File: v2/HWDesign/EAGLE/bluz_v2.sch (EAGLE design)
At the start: 24 parts, among them Q1 FC-12M, U1 MDBT40SMD, U2 SST25VF016B-50-4I-S2AF, U3 MCP1700T-3302E/TT

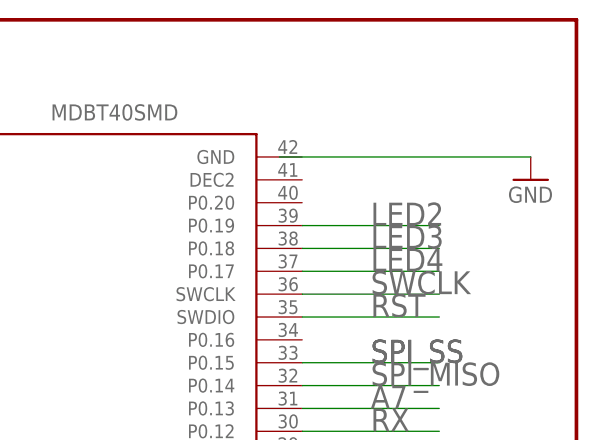
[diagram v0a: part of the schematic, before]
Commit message: fix an issue on the PCB
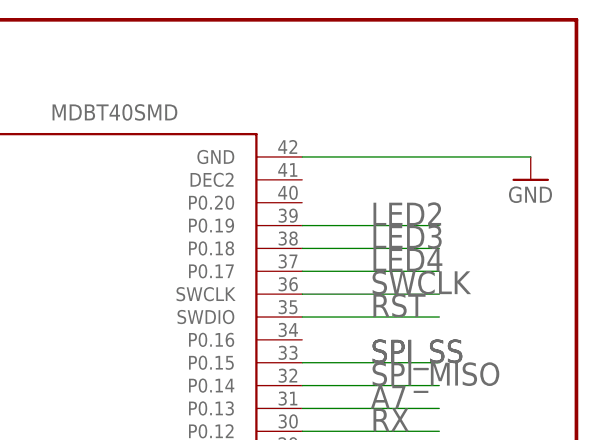
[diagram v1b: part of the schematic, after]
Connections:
- net GND: now also U1.GND@5
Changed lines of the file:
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@@
-</segment>
-<segment>
-<pinref part="GND7" gate="1" pin="GND"/>
-<wire x1="246.38" y1="200.66" x2="274.32" y2="200.66" width="0.1524" layer="91"/>
 </segment>
 <segment>
@@
 <wire x1="193.04" y1="119.38" x2="193.04" y2="124.46" width="0.1524" layer="91"/>
 </segment>
+<segment>
+<pinref part="U1" gate="G$1" pin="GND@5"/>
+<pinref part="GND7" gate="1" pin="GND"/>
+<wire x1="248.92" y1="200.66" x2="274.32" y2="200.66" width="0.1524" layer="91"/>
+</segment>
 </net>

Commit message: larger silkscreen. remove labels. copper on bottom of castellated edges. move buttons further in
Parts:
- removed U2: SST25VF016B-50-4I-S2AF, Silicon_Storage_Tech_By_element14_Batch_1:SST25VF016B-50-4I-S2AF
- added U4: SST25VF010A-33-4I-SAE, Silicon_Storage_Tech_By_element14_Batch_1:SST25VF010A-33-4I-SAE
- R1: value (none) -> 1k
- R6: value (none) -> 10k
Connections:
- net GND: now also U4.VSS; no longer U2.VSS
- net SPI_MISO: now also U4.SO; no longer U2.SO
- net SPI_MOSI: now also U4.SI; no longer U2.SI
- net SPI_SCK: now also U4.SCK; no longer U2.SCK
- net SPI_SS: now also U4.CE; no longer U2.CE
- net VCC: now also U4.HOLD, U4.VDD, U4.WP; no longer U2.HOLD, U2.VDD, U2.WP
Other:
- note added: "C"
- note removed: "A"
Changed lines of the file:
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@@
 <?xml version="1.0" encoding="utf-8"?>
 <!DOCTYPE eagle SYSTEM "eagle.dtd">
-<eagle version="6.5.0">
+<eagle version="7.3.0">
 <drawing>
 <settings>
@@
 <parts>
 <part name="U1" library="MDBT40" deviceset="MDBT40" device="SMD"/>
-<part name="U2" library="Silicon_Storage_Tech_By_element14_Batch_1" deviceset="SST25VF016B-50-4I-S2AF" device="" value=""/>
 <part name="GND1" library="SparkFun-Aesthetics" deviceset="GND" device=""/>
 <part name="C1" library="SparkFun-Capacitors" deviceset="CAP" device="0603-CAP" value="1uF"/>
@@
 <part name="GND3" library="SparkFun-Aesthetics" deviceset="GND" device=""/>
 <part name="C3" library="SparkFun-Capacitors" deviceset="CAP" device="0603-CAP" value=".1uF"/>
-<part name="R1" library="SparkFun-Resistors" deviceset="RESISTOR" device="0603"/>
+<part name="R1" library="SparkFun-Resistors" deviceset="RESISTOR" device="0603" value="1k"/>
 <part name="SUPPLY3" library="SparkFun-Aesthetics" deviceset="VCC" device=""/>
 <part name="GND4" library="SparkFun-Aesthetics" deviceset="GND" device=""/>
@@
 <part name="GND9" library="SparkFun-Aesthetics" deviceset="GND" device=""/>
 <part name="GND10" library="SparkFun-Aesthetics" deviceset="GND" device=""/>
-<part name="R6" library="SparkFun-Passives" deviceset="RESISTOR" device="0603-RES"/>
+<part name="R6" library="SparkFun-Passives" deviceset="RESISTOR" device="0603-RES" value="10k"/>
 <part name="SUPPLY5" library="SparkFun-Aesthetics" deviceset="VCC" device=""/>
 <part name="U3" library="Microchip_By_element14_Batch_1" deviceset="MCP1700T-3302E/TT" device=""/>
@@
 <part name="FRAME1" library="SparkFun-Aesthetics" deviceset="FRAME-LETTER" device=""/>
 <part name="SUPPLY6" library="SparkFun-Aesthetics" deviceset="VCC" device=""/>
+<part name="U4" library="Silicon_Storage_Tech_By_element14_Batch_1" deviceset="SST25VF010A-33-4I-SAE" device=""/>
 </parts>
 <sheets>
@@
 <text x="213.36" y="111.76" size="2.54" layer="95">MDBT40-256R</text>
 <text x="200.66" y="6.35" size="5.08" layer="94">Eric Ely</text>
-<text x="269.494" y="6.35" size="3.81" layer="94">A</text>
+<text x="269.494" y="6.35" size="3.81" layer="94">C</text>
 <text x="195.834" y="16.764" size="3.81" layer="94">Bluz DK v2</text>
 <text x="189.992" y="1.016" size="2.54" layer="94">July 1, 2015</text>
@@
 <instances>
 <instance part="U1" gate="G$1" x="220.98" y="177.8"/>
-<instance part="U2" gate="A" x="63.5" y="139.7"/>
 <instance part="GND1" gate="1" x="27.94" y="175.26"/>
 <instance part="C1" gate="G$1" x="17.78" y="187.96"/>
@@
 </instance>
 <instance part="SUPPLY6" gate="G$1" x="109.22" y="205.74"/>
+<instance part="U4" gate="A" x="63.5" y="139.7"/>
 </instances>
 <busses>
@@
 </segment>
 <segment>
-<pinref part="U2" gate="A" pin="VSS"/>
 <pinref part="GND3" gate="1" pin="GND"/>
 <wire x1="38.1" y1="127" x2="45.72" y2="127" width="0.1524" layer="91"/>
@@
 <junction x="38.1" y="127"/>
 <pinref part="C3" gate="G$1" pin="2"/>
+<pinref part="U4" gate="A" pin="VSS"/>
 </segment>
 <segment>
@@
 <segment>
 <pinref part="SUPPLY2" gate="G$1" pin="VCC"/>
-<pinref part="U2" gate="A" pin="VDD"/>
 <wire x1="7.62" y1="147.32" x2="25.4" y2="147.32" width="0.1524" layer="91"/>
 <wire x1="25.4" y1="147.32" x2="45.72" y2="147.32" width="0.1524" layer="91"/>
@@
 <wire x1="25.4" y1="134.62" x2="25.4" y2="132.08" width="0.1524" layer="91"/>
 <wire x1="25.4" y1="132.08" x2="45.72" y2="132.08" width="0.1524" layer="91"/>
+<junction x="25.4" y="134.62"/>
+<pinref part="C3" gate="G$1" pin="1"/>
 <wire x1="45.72" y1="132.08" x2="48.26" y2="132.08" width="0.1524" layer="91"/>
 <wire x1="48.26" y1="134.62" x2="45.72" y2="134.62" width="0.1524" layer="91"/>
-<junction x="25.4" y="134.62"/>
-<pinref part="C3" gate="G$1" pin="1"/>
 <wire x1="45.72" y1="134.62" x2="25.4" y2="134.62" width="0.1524" layer="91"/>
 <wire x1="7.62" y1="134.62" x2="7.62" y2="137.16" width="0.1524" layer="91"/>
@@
 <wire x1="12.7" y1="137.16" x2="7.62" y2="137.16" width="0.1524" layer="91"/>
 <junction x="7.62" y="137.16"/>
-<pinref part="U2" gate="A" pin="WP"/>
+<pinref part="U4" gate="A" pin="VDD"/>
+<pinref part="U4" gate="A" pin="WP"/>
 <junction x="45.72" y="134.62"/>
-<pinref part="U2" gate="A" pin="HOLD"/>
+<pinref part="U4" gate="A" pin="HOLD"/>
 <junction x="45.72" y="132.08"/>
 </segment>
@@
 <net name="SPI_SS" class="0">
 <segment>
-<pinref part="U2" gate="A" pin="CE"/>
 <pinref part="R1" gate="G$1" pin="2"/>
 <wire x1="45.72" y1="137.16" x2="22.86" y2="137.16" width="0.1524" layer="91"/>
 <label x="33.02" y="137.16" size="1.778" layer="95"/>
+<pinref part="U4" gate="A" pin="CE"/>
 </segment>
 <segment>
@@
 <net name="SPI_MOSI" class="0">
 <segment>
-<pinref part="U2" gate="A" pin="SI"/>
 <wire x1="45.72" y1="142.24" x2="35.56" y2="142.24" width="0.1524" layer="91"/>
 <label x="33.02" y="142.24" size="1.778" layer="95"/>
+<pinref part="U4" gate="A" pin="SI"/>
 </segment>
 <segment>
@@
 <net name="SPI_SCK" class="0">
 <segment>
-<pinref part="U2" gate="A" pin="SCK"/>
 <wire x1="45.72" y1="139.7" x2="35.56" y2="139.7" width="0.1524" layer="91"/>
 <label x="33.02" y="139.7" size="1.778" layer="95"/>
+<pinref part="U4" gate="A" pin="SCK"/>
 </segment>
 <segment>
@@
 <net name="SPI_MISO" class="0">
 <segment>
-<pinref part="U2" gate="A" pin="SO"/>
 <wire x1="81.28" y1="147.32" x2="93.98" y2="147.32" width="0.1524" layer="91"/>
 <label x="83.82" y="147.32" size="1.778" layer="95"/>
-</segment>
-<segment>
+<pinref part="U4" gate="A" pin="SO"/>
+</segment>
+<segment>

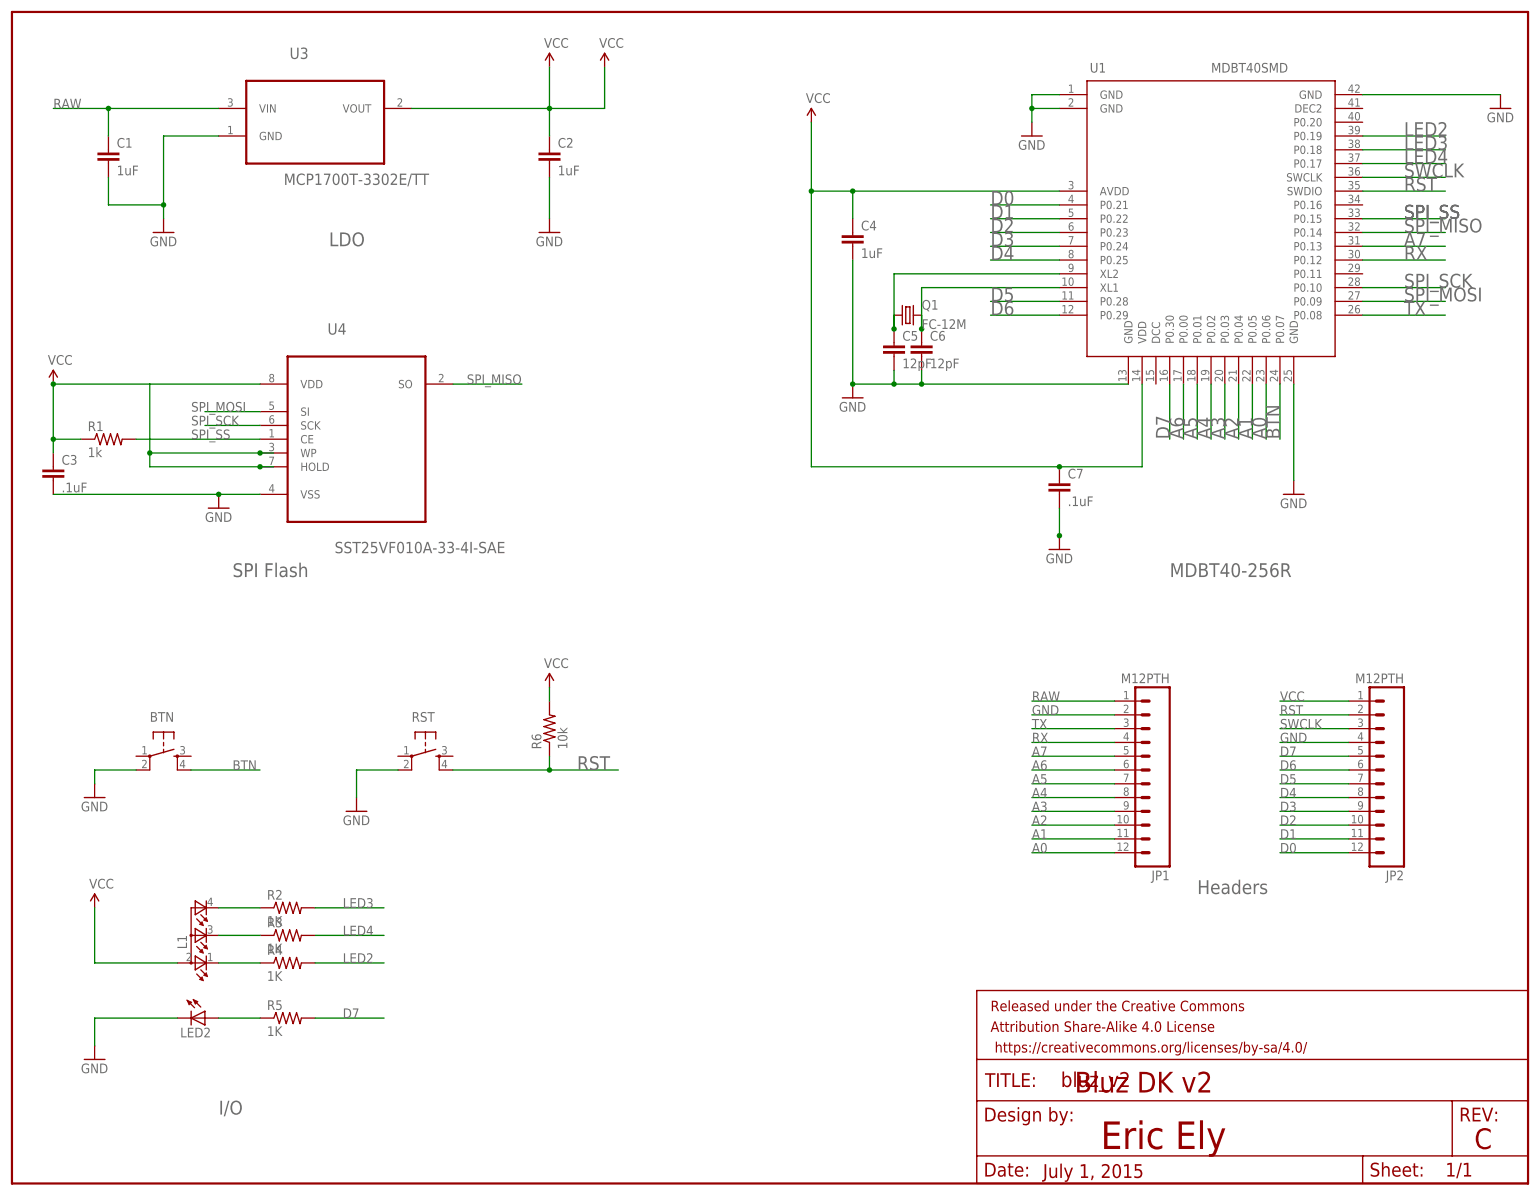
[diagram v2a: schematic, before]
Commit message: updated RGB LED to new part. changed resistors for new LED. updated labeling on bluz.
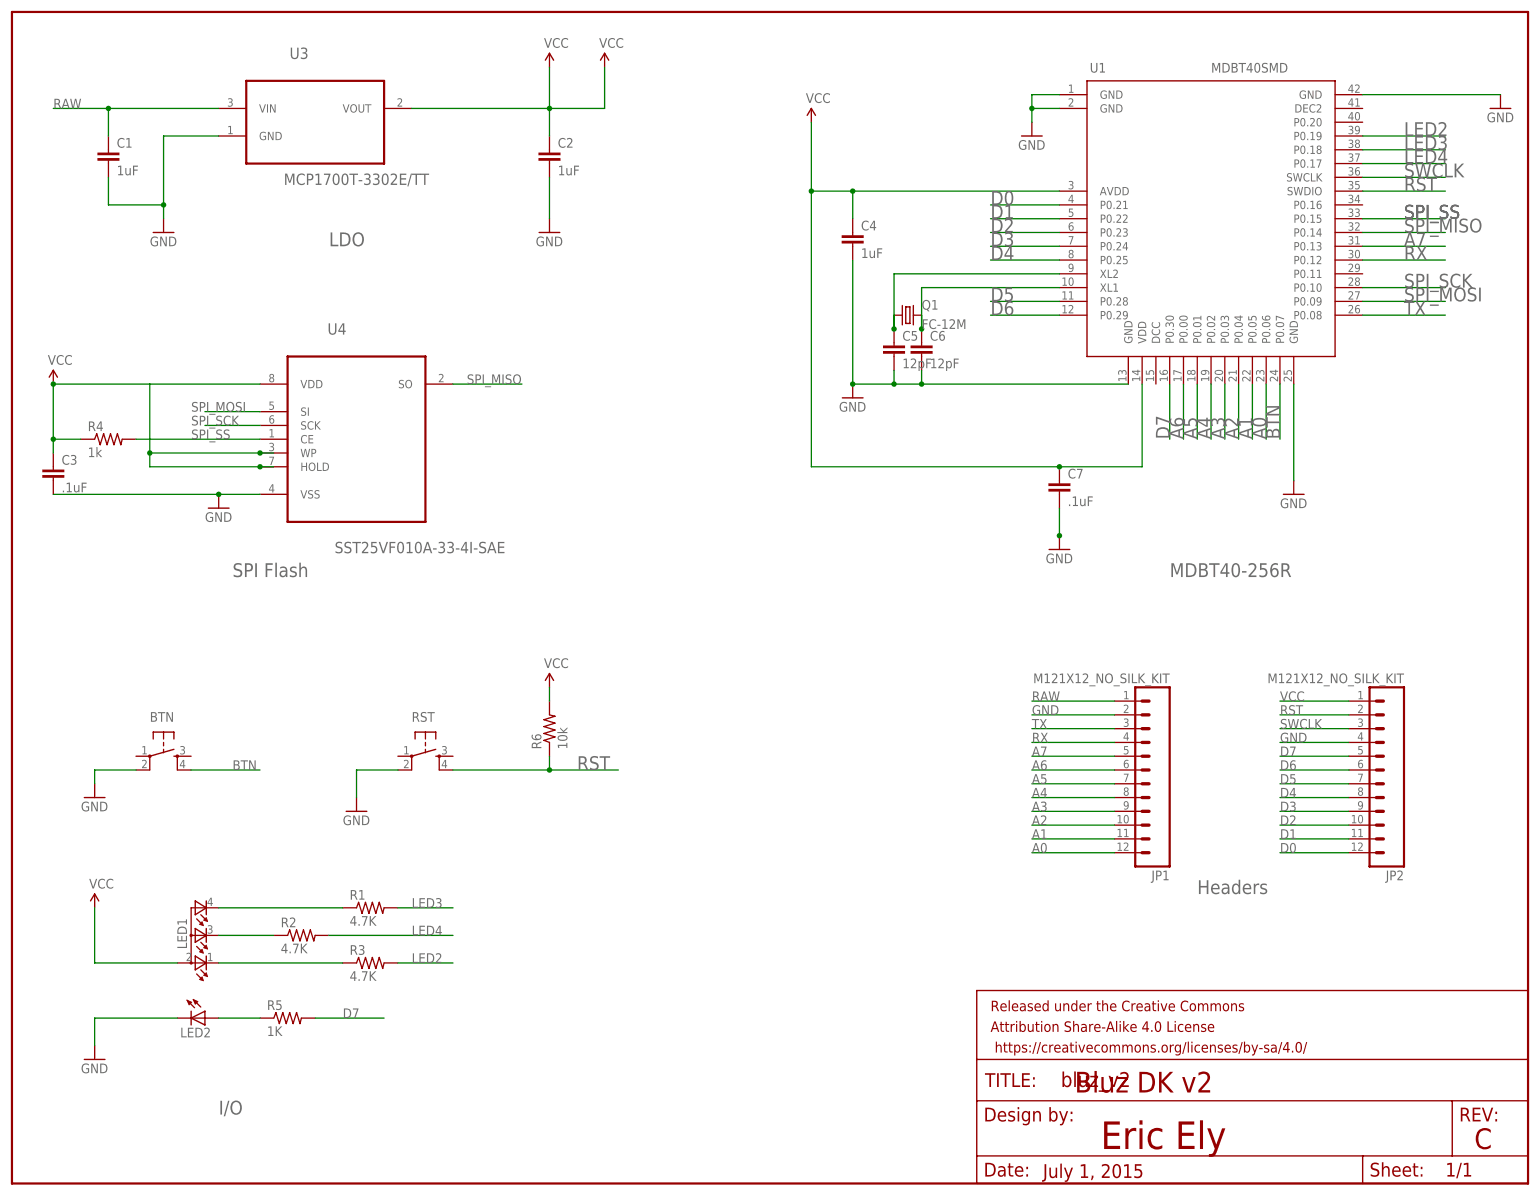
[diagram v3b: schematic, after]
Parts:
- removed L1: (no value), Spark:TOPLED-3PLCC
- added LED1: (no value), bluze_libr:TOPLED-3PLCC
- JP1, JP2: value M12PTH -> M121X12_NO_SILK_KIT; device SparkFun-Connectors:M12PTH -> SparkFun-Connectors:M121X12_NO_SILK_KIT
- R1: value 1k -> 4.7K; device SparkFun-Resistors:RESISTOR0603 -> SparkFun-Passives:RESISTOR0603-RES
- R2, R3: value 1K -> 4.7K
- R4: value 1K -> 1k; device SparkFun-Passives:RESISTOR0603-RES -> SparkFun-Resistors:RESISTOR0603
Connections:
- net LED2: now also R3.2; no longer R4.2
- net LED3: now also R1.2; no longer R2.2
- net LED4: now also R2.2; no longer R3.2
- net N$5: now also LED1.CRED, R3.1; no longer L1.CRED, R4.1
- net N$6: now also LED1.CBLUE, R2.1; no longer L1.CBLUE, R3.1
- net N$7: now also LED1.CGREEN, R1.1; no longer L1.CGREEN, R2.1
- net SPI_SS: now also R4.2; no longer R1.2
- net VCC: now also LED1.A2, R4.1; no longer L1.A2, R1.1
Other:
- moved on the sheet: R1, R2, R3, R4

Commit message: cleanup some naming mistakes. properly labeled all capacitors
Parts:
- C3: value .1uF -> 1uF
- C4: value 1uF -> .1uF
- C5: value 12pF -> .1uF
- C7: value .1uF -> 12pF
- renumbered BTN to S1, LED1 to L1, LED2 to L2, RST to S2, U4 to U2
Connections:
- net N$2: now also C7.1; no longer C5.1
- net VCC: now also C5.1; no longer C7.1
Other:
- moved on the sheet: C3, C4, C5, C7
